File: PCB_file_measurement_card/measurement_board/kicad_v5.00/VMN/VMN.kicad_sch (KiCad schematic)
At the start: 41 parts, among them J1 A/B, J10 Conn_01x08_Female, J11 Conn_01x02_Female, J12 Conn_01x02_Female, J13 Conn_01x08_Female, J2 Screw_Terminal_VMN, J3 Alim DPH5005, J4 Conn_01x08_Female, J5 Conn_01x04_Female, J6 Conn_01x08_Female, J7 Raspberry_Pi_2_3, J8 Conn_02x03_Top_Bottom, K1 AQY211EH, K2 AQY211EH, K3 AQY211EH, K4 AQY211EH, U1 INA128, U2 MCP23008-xP, U3 LM358, U5 1085-Adress=0X49, U6 1085-Adress=0X48

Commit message: correction kicad V5.00
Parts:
- removed C10, C3, C6, C9: 10uF, Capacitor_THT:CP_Radial_D6.3mm_P2.50mm, symbol Device:C_Polarized_Small
- removed C4, C5, C7, C8: 100nF, Capacitor_THT:C_Disc_D8.0mm_W2.5mm_P5.00mm, symbol Device:C_Small
- removed D1, D2, D3, D4: BAT86, Diode_THT:D_DO-35_SOD27_P7.62mm_Horizontal, symbol Diode:BAT86
- removed J10, J13: Conn_01x08_Female, Connector_PinHeader_2.54mm:PinHeader_1x08_P2.54mm_Vertical, symbol Connector:Conn_01x08_Female
- removed J11: Conn_01x02_Female, symbol Connector:Conn_01x02_Female
- removed J12: Conn_01x02_Female, Connector_PinHeader_2.54mm:PinHeader_1x02_P2.54mm_Vertical, symbol Connector:Conn_01x02_Female
- removed J2: Screw_Terminal_VMN, TerminalBlock_Phoenix:TerminalBlock_Phoenix_MKDS-1,5-2-5.08_1x02_P5.08mm_Horizontal, symbol Connector:Screw_Terminal_01x02
- removed J3: Alim DPH5005, TerminalBlock_Phoenix:TerminalBlock_Phoenix_MKDS-1,5-2-5.08_1x02_P5.08mm_Horizontal, symbol Connector:Screw_Terminal_01x02
- removed K1, K2, K3, K4: AQY211EH, AQY211EH:DIP762W47P254L478H340Q4N, symbol AQY211EH:AQY211EH
- removed R1, R2: 1.5k, Resistor_THT:R_Axial_DIN0207_L6.3mm_D2.5mm_P7.62mm_Horizontal, symbol Device:R
- removed R3, R4, R5: 1k, Resistor_THT:R_Axial_DIN0207_L6.3mm_D2.5mm_P7.62mm_Horizontal, symbol Device:R
- removed R6: 2, Resistor_THT:R_Axial_DIN0414_L11.9mm_D4.5mm_P20.32mm_Horizontal, symbol Device:R
- removed U1: INA128, Package_DIP:DIP-8_W7.62mm, symbol Amplifier_Instrumentation:INA128
- removed U2: MCP23008-xP, Package_DIP:DIP-18_W7.62mm, symbol Interface_Expansion:MCP23008-xP
- removed U3: LM358, Package_DIP:DIP-8_W7.62mm, symbol Amplifier_Operational:LM358
- removed U5: 1085-Adress=0X49, 1085:1085, symbol 1085:1085
- removed U6: 1085-Adress=0X48, 1085:1085, symbol 1085:1085
- added J16: RX_bat, TerminalBlock_Phoenix:TerminalBlock_Phoenix_MKDS-1,5-2-5.08_1x02_P5.08mm_Horizontal, symbol Connector:Screw_Terminal_01x02
- added J9: TX_bat, TerminalBlock_Phoenix:TerminalBlock_Phoenix_MKDS-1,5-2-5.08_1x02_P5.08mm_Horizontal, symbol Connector:Screw_Terminal_01x02
- added U1: MCP23008-xP, Package_DIP:DIP-18_W7.62mm, symbol Interface_Expansion:MCP23008-xP
- J1: value A/B -> DSP_out_12v_GND
- J8: value Conn_02x03_Top_Bottom -> Connector_I2C_for_mux_or_tools
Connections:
- net 5VD: now also U1.18 (VDD), U1.6 (~{RESET})
- net GNDD: now also U1.3 (A2), U1.4 (A1), U1.5 (A0), U1.9 (VSS)
- net SCL1: now also U1.1 (SCL)
- net SDA1: now also U1.2 (SDA)
- net 5V renamed 5VA
- net A renamed Relay_switch_dsp/out_GND_DSP
- net B renamed Relay_switch_dsp/out_12v_DSP
- new net +12V: J16.1 (Pin_1), J9.1 (Pin_1)
- new net GNDPWR: J16.2 (Pin_2), J9.2 (Pin_2)
- new net GP2: U1.12 (GP2)
- new net GP3: U1.13 (GP3)
- no-connect marks 73 -> 47
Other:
- sheet Alim renamed Alimentation
- added sheet Current_injection_and_measurement (Current_injection_and_measurement.kicad_sch)
- added sheet Relay_switch_dsp (Relay_switch_dsp.kicad_sch)
- added sheet Vmn_measurement (Vmn_measurement.kicad_sch)
- sheet Alimentation ports: added +12V_A, -12V_A, 12V_Power, 5V_A, 5V_D, Common_A, GND_D, GND_Power; removed none
- note removed: "J'ai fixé R9 et R10 à 1.5 kohm comme dans la v2.00"
- title: (none) -> Ohmpi_measurement_board
- moved on the sheet: J4, J5, J6, J7, J8

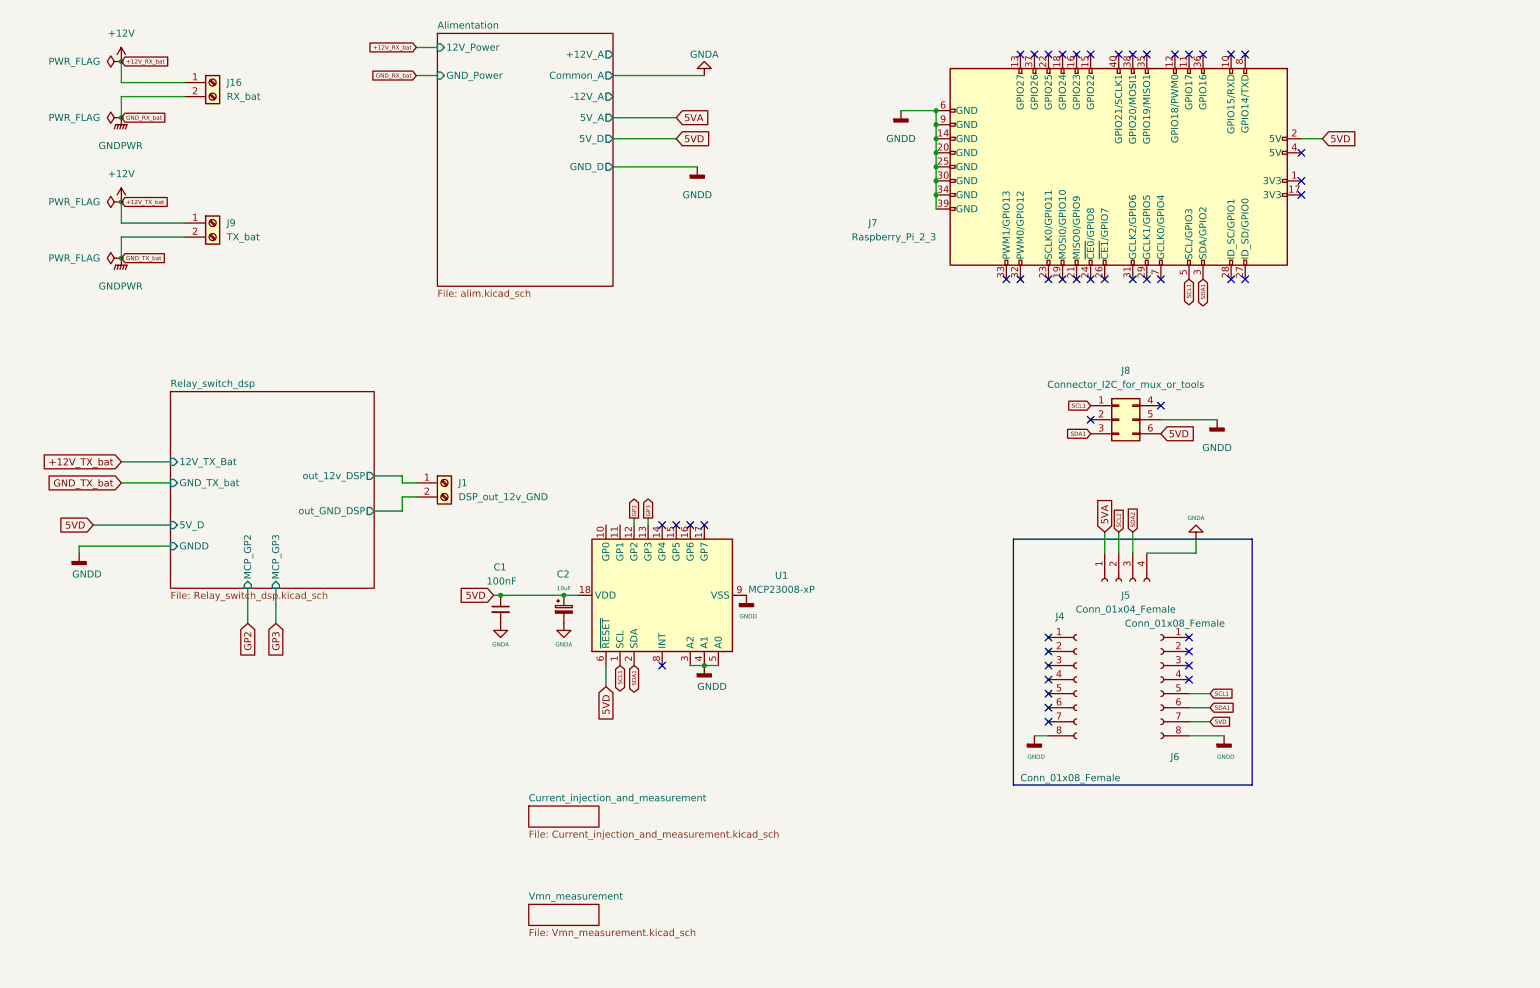
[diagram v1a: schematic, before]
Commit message: new schematics for V5.00
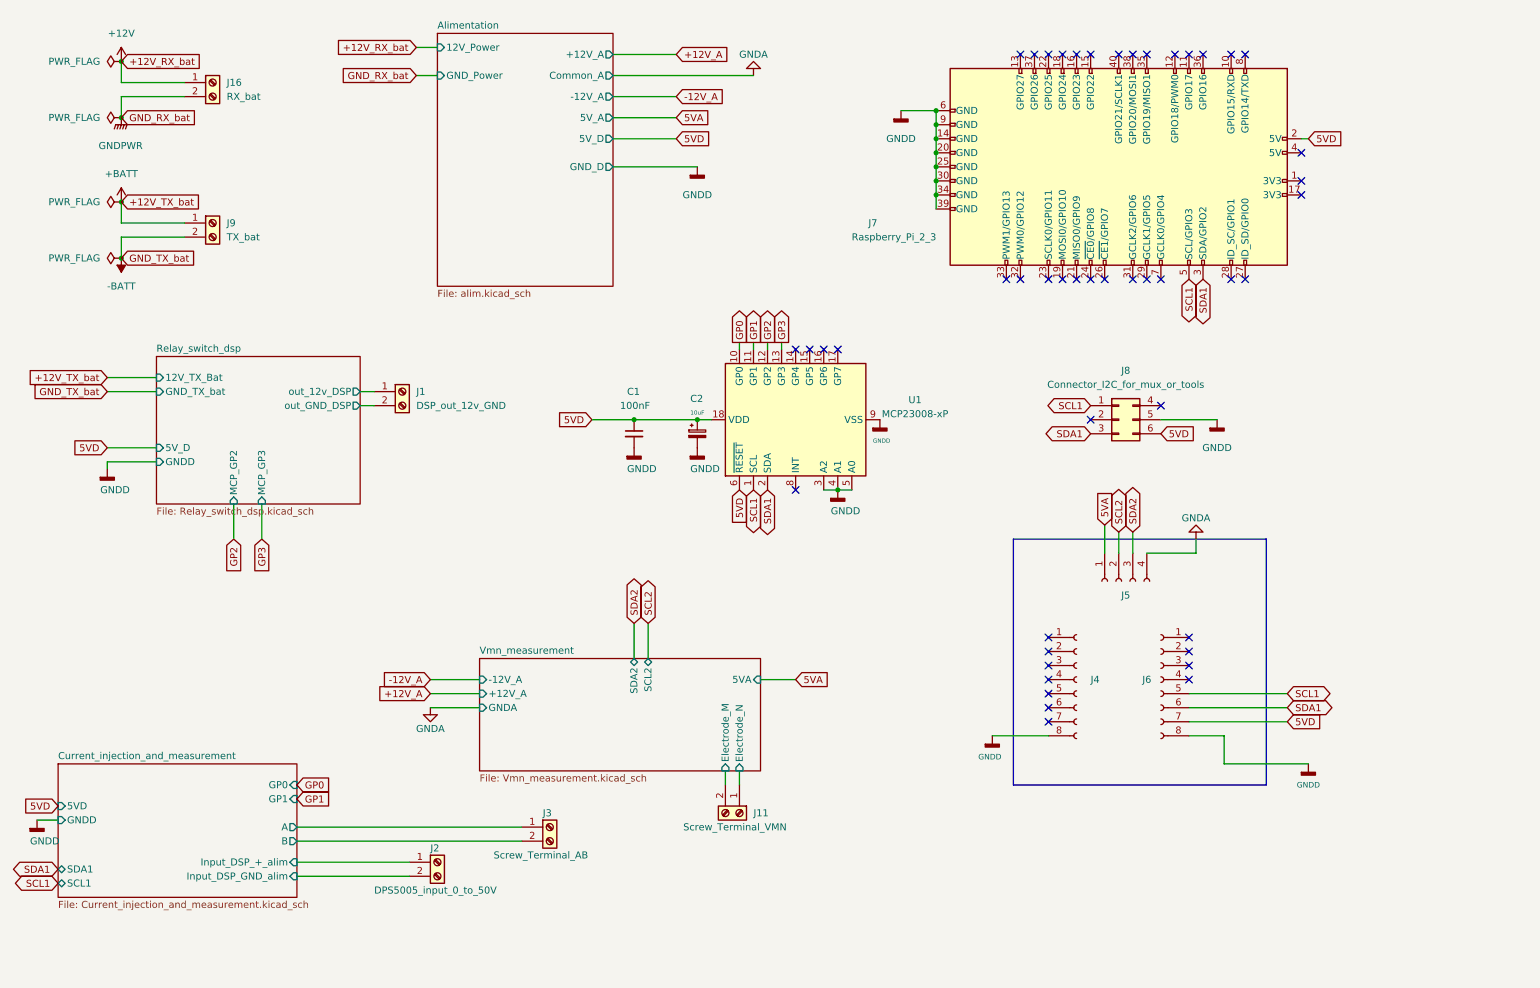
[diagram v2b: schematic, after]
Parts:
- added J11: Screw_Terminal_VMN, TerminalBlock_Phoenix:TerminalBlock_Phoenix_MKDS-1,5-2-5.08_1x02_P5.08mm_Horizontal, symbol Connector:Screw_Terminal_01x02
- added J2: DPS5005_input_0_to_50V, TerminalBlock_Phoenix:TerminalBlock_Phoenix_MKDS-1,5-2-5.08_1x02_P5.08mm_Horizontal, symbol Connector:Screw_Terminal_01x02
- added J3: Screw_Terminal_AB, TerminalBlock_Phoenix:TerminalBlock_Phoenix_MKDS-1,5-2-5.08_1x02_P5.08mm_Horizontal, symbol Connector:Screw_Terminal_01x02
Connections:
- net +12V: no longer J9.1 (Pin_1)
- net GNDA: no longer C1.2, C2.2
- net GNDD: now also C1.2, C2.2
- net GNDPWR: no longer J9.2 (Pin_2)
- net GP0: now reaches U1.10 (GP0)
- net GP1: now reaches U1.11 (GP1)
- new net +BATT: J9.1 (Pin_1)
- new net -BATT: J9.2 (Pin_2)
- new net Current_injection_and_measurement/A: J3.1 (Pin_1)
- new net Current_injection_and_measurement/B: J3.2 (Pin_2)
- new net Current_injection_and_measurement/Input_DSP_+_alim: J2.1 (Pin_1)
- new net Current_injection_and_measurement/Input_DSP_GND_alim: J2.2 (Pin_2)
- new net Vmn_measurement/Electrode_M: J11.2 (Pin_2)
- new net Vmn_measurement/Electrode_N: J11.1 (Pin_1)
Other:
- sheet Current_injection_and_measurement ports: added 5VD, A, B, GNDD, GP0, GP1, Input_DSP_+_alim, Input_DSP_GND_alim, SCL1, SDA1; removed none
- sheet Vmn_measurement ports: added +12V_A, -12V_A, 5VA, Electrode_M, Electrode_N, GNDA, SCL2, SDA2; removed none
- moved on the sheet: C1, C2, J1, U1

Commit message: last version of measurement board, with op07
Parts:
- added J10: DSP+, Connector_PinHeader_2.54mm:PinHeader_1x01_P2.54mm_Vertical, symbol Connector_Generic:Conn_01x01
- added J17: DSP GND, Connector_PinHeader_2.54mm:PinHeader_1x01_P2.54mm_Vertical, symbol Connector_Generic:Conn_01x01
- added J18, J19: Conn_01x01, Connector_PinHeader_2.54mm:PinHeader_1x01_P2.54mm_Vertical, symbol Connector_Generic:Conn_01x01
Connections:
- net Vmn_measurement/Electrode_N is gone; now on net GNDA: J11.1 (Pin_1)
- net Current_injection_and_measurement/Input_DSP_+_alim: now also J10.1 (Pin_1)
- net Current_injection_and_measurement/Input_DSP_GND_alim: now also J17.1 (Pin_1)
- net GNDA: now also J19.1 (Pin_1)
- net Vmn_measurement/Electrode_M: now also J18.1 (Pin_1)
- net GP4: now reaches U1.14 (GP4)
- net GP5: now reaches U1.15 (GP5)
- net GP6: now reaches U1.16 (GP6)
- net GP7: now reaches U1.17 (GP7)
- no-connect marks 47 -> 43
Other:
- added sheet IHM (IHM.kicad_sch)
- sheet Vmn_measurement ports: added none; removed Electrode_N
- moved on the sheet: J11
